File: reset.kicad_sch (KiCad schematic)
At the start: 8 parts, among them J3 RESET

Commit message: board layout
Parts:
- C2: footprint Capacitor_SMD:C_0805_2012Metric_Pad1.18x1.45mm_HandSolder -> Capacitor_THT:C_Disc_D4.3mm_W1.9mm_P5.00mm
- C3: footprint Capacitor_SMD:CP_Elec_4x4.5 -> Capacitor_THT:CP_Radial_D8.0mm_P5.00mm
- D1, D2, D3: footprint Diode_SMD:D_SOD-323_HandSoldering -> Diode_THT:D_DO-34_SOD68_P7.62mm_Horizontal
- R3, R4: footprint Resistor_SMD:R_0805_2012Metric_Pad1.20x1.40mm_HandSolder -> Resistor_THT:R_Axial_DIN0204_L3.6mm_D1.6mm_P2.54mm_Vertical
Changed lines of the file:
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@@
 			)
 		)
-		(property "Footprint" "Capacitor_SMD:C_0805_2012Metric_Pad1.18x1.45mm_HandSolder"
+		(property "Footprint" "Capacitor_THT:C_Disc_D4.3mm_W1.9mm_P5.00mm"
 			(at 127 101.6 0)
 			(effects
@@
 			)
 		)
-		(property "Footprint" "Resistor_SMD:R_0805_2012Metric_Pad1.20x1.40mm_HandSolder"
+		(property "Footprint" "Resistor_THT:R_Axial_DIN0204_L3.6mm_D1.6mm_P2.54mm_Vertical"
 			(at 136.652 91.44 90)
 			(effects
@@
 			)
 		)
-		(property "Footprint" "Diode_SMD:D_SOD-323_HandSoldering"
+		(property "Footprint" "Diode_THT:D_DO-34_SOD68_P7.62mm_Horizontal"
 			(at 121.285 91.44 0)
 			(effects
@@
 			)
 		)
-		(property "Footprint" "Diode_SMD:D_SOD-323_HandSoldering"
+		(property "Footprint" "Diode_THT:D_DO-34_SOD68_P7.62mm_Horizontal"
 			(at 122.555 91.44 0)
 			(effects
@@
 			)
 		)
-		(property "Footprint" "Capacitor_SMD:CP_Elec_4x4.5"
+		(property "Footprint" "Capacitor_THT:CP_Radial_D8.0mm_P5.00mm"
 			(at 159.512 92.71 0)
 			(effects
@@
 			)
 		)
-		(property "Footprint" "Diode_SMD:D_SOD-323_HandSoldering"
+		(property "Footprint" "Diode_THT:D_DO-34_SOD68_P7.62mm_Horizontal"
 			(at 112.395 101.6 0)
 			(effects
@@
 			)
 		)
-		(property "Footprint" "Resistor_SMD:R_0805_2012Metric_Pad1.20x1.40mm_HandSolder"
+		(property "Footprint" "Resistor_THT:R_Axial_DIN0204_L3.6mm_D1.6mm_P2.54mm_Vertical"
 			(at 157.734 81.28 90)
 			(effects

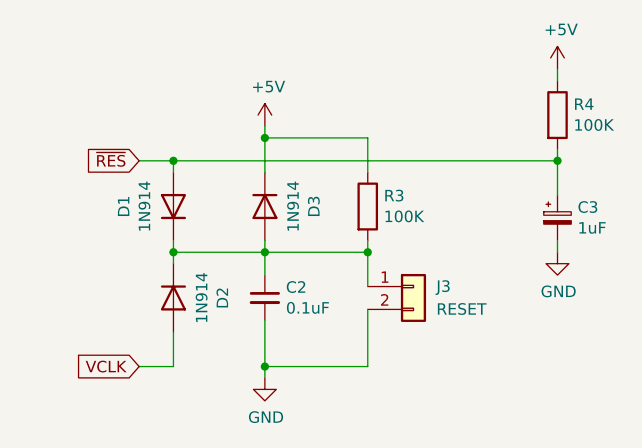
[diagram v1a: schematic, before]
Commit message: revise bus tracing
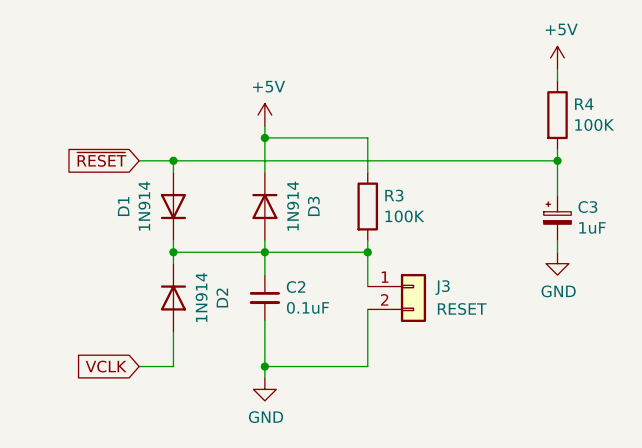
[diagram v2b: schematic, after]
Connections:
- net ~{RES} renamed ~{RESET}
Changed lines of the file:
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@@
 		)
 	)
-	(global_label "~{RES}"
+	(global_label "~{RESET}"
 		(shape input)
 		(at 113.03 86.36 180)
@@
 		)
 		(property "Intersheetrefs" "${INTERSHEET_REFS}"
-			(at 107.0772 86.4394 0)
+			(at 104.2997 86.36 0)
 			(effects
 				(font
 					(size 1.27 1.27)
 				)
-				(justify left)
+				(justify right)
 				(hide yes)
 			)
